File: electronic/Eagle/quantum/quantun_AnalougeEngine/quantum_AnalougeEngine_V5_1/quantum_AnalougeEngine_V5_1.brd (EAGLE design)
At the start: 210 x 70 mm, 307 parts, among them IC1 OP275, IC10 STM32F767ZIT6, IC12 ESDA6V1BC6, IC13 USBLC6-4SC6, IC14 TL072, IC15 TL072, IC16 OP275, IC17 AD7606BSTZ-6, IC2 DAC084S085CIMM_NOPB, IC3 DAC084S085CIMM_NOPB, IC4 OP275, IC5 OP275, IC6 LAN8742A-CZ-TR, IC7 TL072, IC8 OP275, IC9 TL072, J1 GWLEX-SMT-S988G_Y, K1 Relay, K2 Relay, K3 Relay, K4 Relay, K5 Relay, K6 Relay, K7 Relay, K8 Relay, T1 H1102NL, U1 78*_SMD, U12 ULN2003, U4 THAT1240, U6 THAT1240, U7 THAT1240, U8 THAT1240, Y1 NX3215SA-32.768K-STD-MUA-8, Y2 NX3225GD-8MHZ-STD-CRA-3, Y3 ABLS2-25.000MHZ-D4YF-T

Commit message: finished Routing: AnalougeEngine_V5_1
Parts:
- removed DISPLAY2: 90814-0204, electro_mechanical:MOLEX_90814-0204
- moved C107 41.4 mm to (50.8, 51.9), turned to 90 degrees
- moved C106 38.7 mm to (49.0, 51.9), turned to 90 degrees
- moved D2 32.8 mm to (48.2, 37.5)
- moved D8 31.8 mm to (22.2, 37.5)
- moved D9 30.0 mm to (22.2, 44.3)
- moved D5 30.0 mm to (22.2, 47.7)
- moved D3 29.0 mm to (48.2, 40.9)
- moved D1 28.9 mm to (48.2, 47.7)
- moved D10 28.5 mm to (22.2, 40.9)
- moved D4 26.4 mm to (48.2, 44.3)
- moved C109 25.1 mm to (24.8, 52.2), turned to 90 degrees
- moved R56 24.3 mm to (116.3, 26.8), turned to 270 degrees
- moved C99 23.6 mm to (120.2, 22.8)
- moved R57 22.8 mm to (127.5, 27.9), turned to 180 degrees
- moved C57 22.1 mm to (122.2, 23.4), turned to 270 degrees
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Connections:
- removed net +5VVVV: R67.2
- net +5V: no longer DISPLAY2.3
- net +5V(ANALOG): now also R67.2
- net CHASIS: no longer C15.1, C18.1
- net CHASSIS: now also C15.1, C18.1
- net DISPLAY_GND_TO_STAR: no longer DISPLAY2.4
- net R/S_OUT+: now also C111.2
- net R/S_OUT-: no longer C111.2
- net USART1_RX: no longer DISPLAY2.2
- net USART1_TX: no longer DISPLAY2.1
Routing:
- net CHASSIS: track 0.00 -> 305.1 mm, vias 0 -> 4
- net AGND: track 78.5 -> 270.9 mm, vias 47 -> 157
- net OUT1_DRIVER: track 0.00 -> 191.5 mm, vias 0 -> 3
- net OUT4_DRIVER: track 0.00 -> 185.6 mm, vias 0 -> 2
- net OUT5_DRIVER: track 0.00 -> 173.9 mm, vias 0 -> 4
- net OUT6_DRIVER: track 0.00 -> 162.4 mm, vias 0 -> 4
- net OUT2_DRIVER: track 0.00 -> 133.8 mm, vias 0 -> 4
- net A_GND_TO_STAR: track 0.00 -> 131.7 mm
- net L/M_OUT(OUT_STAGE_LEFT)_BEFORE: track 0.00 -> 104.2 mm, vias 0 -> 4
- net L/M_OUT(VCA1_OUT): track 0.00 -> 99.2 mm, vias 0 -> 2
- net R/S_OUT(VCA2_OUT): track 0.00 -> 97.6 mm, vias 0 -> 2
- net N$59: track 0.00 -> 94.6 mm, vias 0 -> 2
- net OUT3_DRIVER: track 0.00 -> 94.4 mm, vias 0 -> 2
- net R/S_OUT(OUT_STAGE_RIGHT)_BEFORE: track 0.00 -> 92.6 mm, vias 0 -> 2
- net E+_OUT_STAGE_RIGHT: track 0.00 -> 92.5 mm, vias 0 -> 1
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
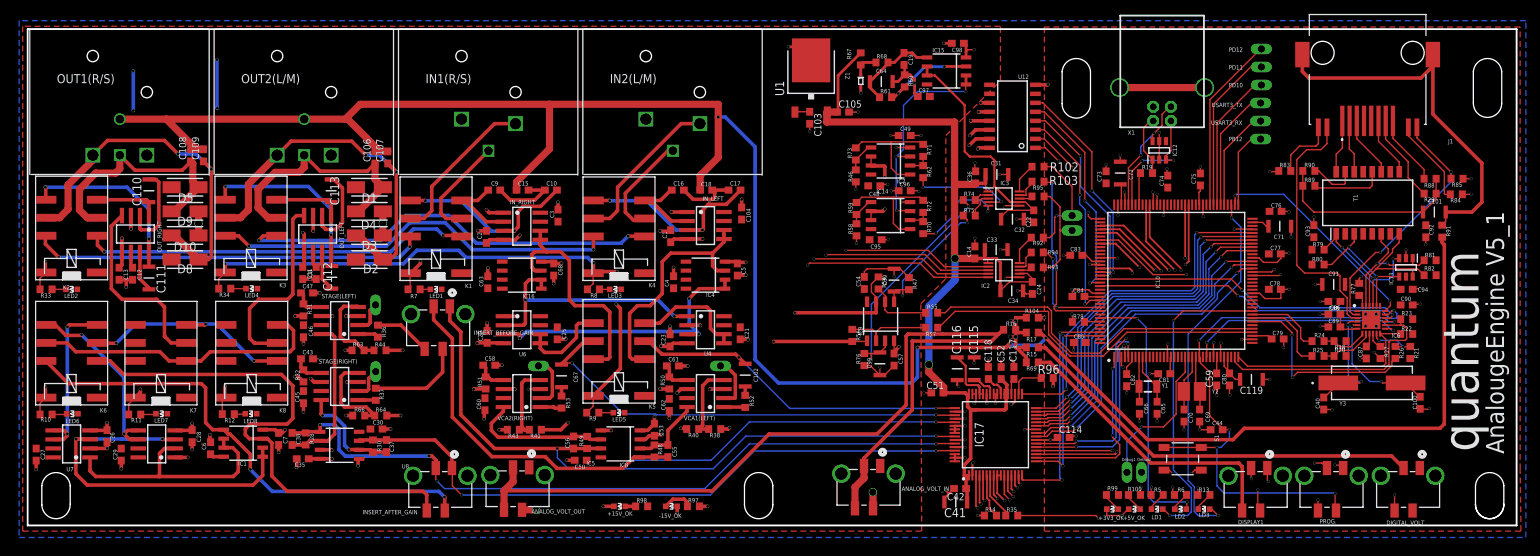
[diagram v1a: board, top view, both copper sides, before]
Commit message: finished all boards s for next PCBway production
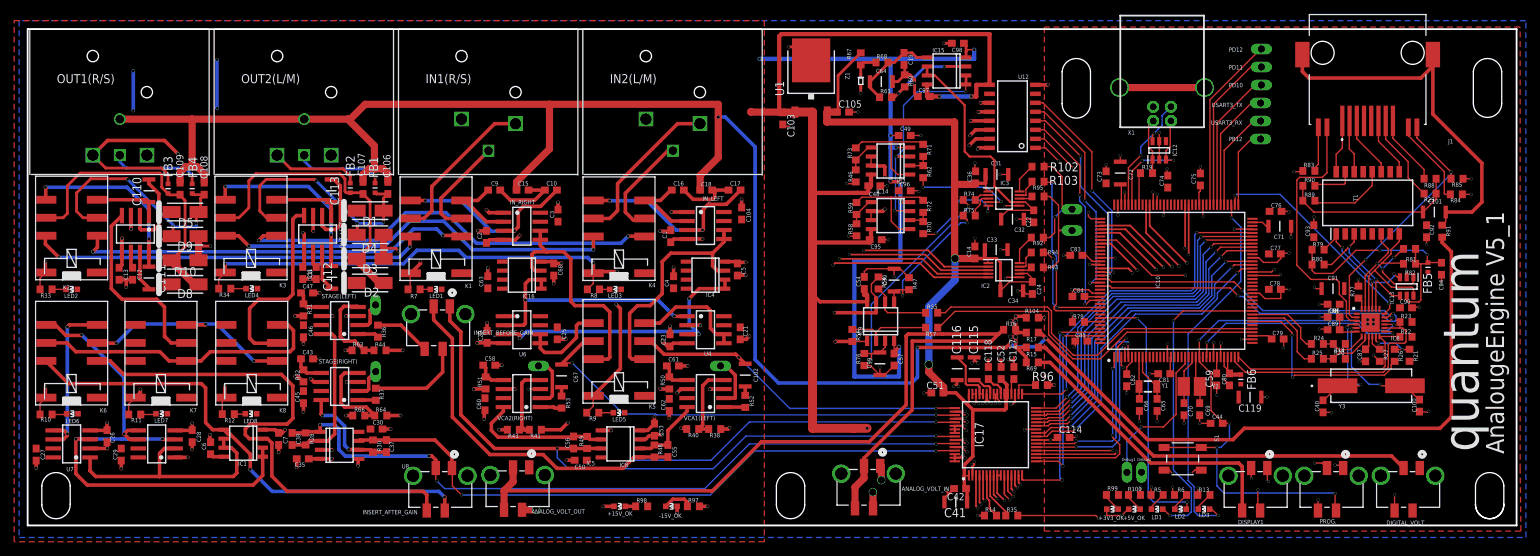
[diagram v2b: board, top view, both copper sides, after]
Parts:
- added FB1, FB2, FB3, FB4, FB6: FERITTE-BREAD, passive components:BLM18KG102SH1J
- added FB5: 0 R, passive components:BLM18KG102SH1J
- moved C109 5.74 mm to (21.5, 47.5)
- moved C94 5.69 mm to (199.4, 36.2), turned to 90 degrees
- moved C107 5.54 mm to (47.3, 47.6)
- moved C108 5.07 mm to (24.9, 47.5)
- moved C106 4.66 mm to (50.8, 47.6)
- moved C103 3.80 mm to (106.5, 57.4)
- moved D10 3.50 mm to (22.2, 37.4)
- moved D5 3.50 mm to (22.2, 44.2)
- moved D8 3.50 mm to (22.2, 34.0)
- moved D9 3.50 mm to (22.2, 40.8)
- moved R83 3.40 mm to (180.7, 50.0)
- moved R81 3.31 mm to (194.9, 39.0)
- moved R82 3.31 mm to (194.9, 36.9)
- moved D1 3.30 mm to (48.3, 44.4)
- moved D2 3.30 mm to (48.3, 34.2)
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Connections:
- removed net +12V: DIGITAL_VOLT.2
- new net N$106: C80.2, FB6.2, IC10.32, IC10.33
- new net N$41: C94.2, FB5.2, IC13.5, R79.2, R80.2, R81.2, R82.2
- new net N$42: FB1.2, OUT2(L/M).3
- new net N$44: FB4.2, OUT1(R/S).3
- new net N$47: C107.1, D2.2, D3.1, FB2.1, K3.P2
- new net N$85: C109.1, D10.1, D8.2, FB3.1, K2.P2
- net +3V3: now also FB5.1, FB6.1; no longer C80.2, C94.2, IC10.32, IC10.33, IC13.5, R79.2, R80.2, R81.2, R82.2
- net NEGATIVE_OUT(L/M): now also FB1.1; no longer OUT2(L/M).3
- net NGATIVE_OUT(R/S): now also FB4.1; no longer OUT1(R/S).3
- net POSITIVE_OUT(L/M): now also FB2.2; no longer C107.1, D2.2, D3.1, K3.P2
- net POSITIVE_OUT(R/S): now also FB3.2; no longer C109.1, D10.1, D8.2, K2.P2
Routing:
- net V+: track 8.58 -> 170.7 mm, vias 0 -> 4
- net V-: track 83.8 -> 213.8 mm, vias 32 -> 34
- net N$47: track 0.00 -> 42.1 mm
- net N$85: track 0.00 -> 41.9 mm
- net POSITIVE_OUT(L/M): track 53.2 -> 12.5 mm, vias 2 -> 0
- net N$41: track 0.00 -> 35.8 mm, vias 0 -> 2
- net POSITIVE_OUT(R/S): track 53.0 -> 26.7 mm, vias 2 -> 1
- net AGND: track 270.9 -> 287.5 mm, vias 157 -> 175
- net N$44: track 0.00 -> 13.1 mm, vias 0 -> 1
- net N$42: track 0.00 -> 12.7 mm, vias 0 -> 1
- net CHASSIS: track 305.1 -> 317.4 mm
- net +3V3: track 27.1 -> 20.4 mm
- net N$106: track 0.00 -> 6.71 mm
- net N$57: track 78.2 -> 84.3 mm
- net N$56: track 54.2 -> 59.3 mm
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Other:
- outline, holes or cut-outs redrawn
